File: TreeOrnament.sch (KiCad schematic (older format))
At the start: 29 parts, among them J1 USB_B_Micro

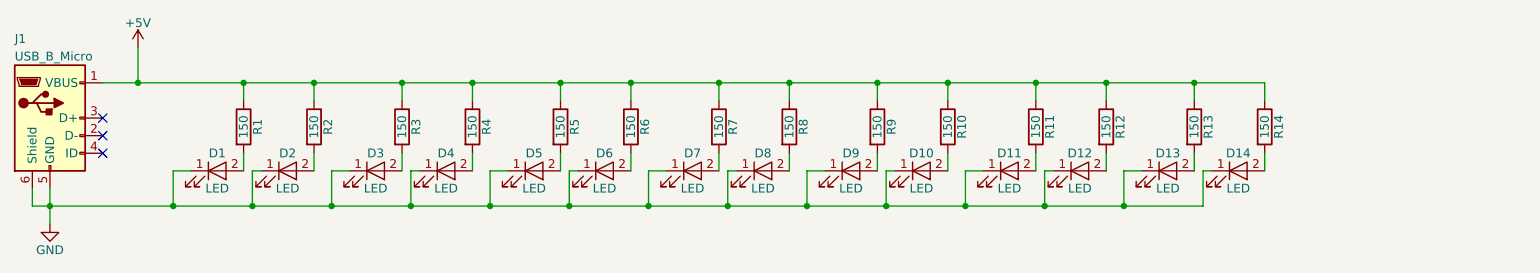
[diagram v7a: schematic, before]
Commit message: Add some optional SMT decoupling caps.
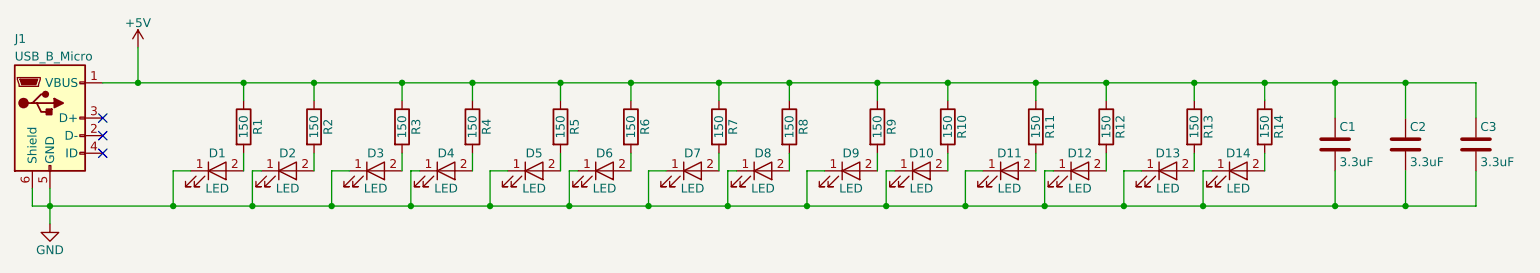
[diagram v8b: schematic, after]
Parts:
- added C1, C2, C3: 3.3uF, Capacitors_SMD:C_0805_HandSoldering, symbol C
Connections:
- net +5V: now also C1.1, C2.1, C3.1
- net GND: now also C1.2, C2.2, C3.2
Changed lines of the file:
@@
 encoding utf-8
 Sheet 1 1
-Title ""
-Date ""
-Rev ""
-Comp ""
+Title "Christmas Tree Ornament"
+Date "2017-11-02"
+Rev "1.1"
+Comp "Patrick Pelletier"
 Comment1 ""
 Comment2 ""
@@
 Connection ~ 6700 1900
 Wire Wire Line
-	1400 1900 8050 1900
-Wire Wire Line
-	1800 1200 8400 1200
+	1400 1900 9600 1900
+Wire Wire Line
+	1800 1200 9600 1200
 $Comp
 L R R1
@@
 	8050 1700 8050 1900
 Connection ~ 7600 1900
+$Comp
+L C C1
+U 1 1 59FBC6D7
+P 8800 1550
+F 0 "C1" H 8825 1650 50  0000 L CNN
+F 1 "3.3uF" H 8825 1450 50  0000 L CNN
+F 2 "Capacitors_SMD:C_0805_HandSoldering" H 8838 1400 50  0001 C CNN
+F 3 "" H 8800 1550 50  0001 C CNN
+	1    8800 1550
+	1    0    0    -1
+$EndComp
+$Comp
+L C C2
+U 1 1 59FBC804
+P 9200 1550
+F 0 "C2" H 9225 1650 50  0000 L CNN
+F 1 "3.3uF" H 9225 1450 50  0000 L CNN
+F 2 "Capacitors_SMD:C_0805_HandSoldering" H 9238 1400 50  0001 C CNN
+F 3 "" H 9200 1550 50  0001 C CNN
+	1    9200 1550
+	1    0    0    -1
+$EndComp
+$Comp
+L C C3
+U 1 1 59FBC875
+P 9600 1550
+F 0 "C3" H 9625 1650 50  0000 L CNN
+F 1 "3.3uF" H 9625 1450 50  0000 L CNN
+F 2 "Capacitors_SMD:C_0805_HandSoldering" H 9638 1400 50  0001 C CNN
+F 3 "" H 9600 1550 50  0001 C CNN
+	1    9600 1550
+	1    0    0    -1
+$EndComp
+Wire Wire Line
+	8800 1200 8800 1400
+Connection ~ 8400 1200
+Wire Wire Line
+	9200 1200 9200 1400
+Connection ~ 8800 1200
+Wire Wire Line
+	9600 1200 9600 1400
+Connection ~ 9200 1200
+Wire Wire Line
+	9600 1900 9600 1700
+Connection ~ 8050 1900
+Wire Wire Line
+	8800 1700 8800 1900
+Connection ~ 8800 1900
+Wire Wire Line
+	9200 1700 9200 1900
+Connection ~ 9200 1900
 $EndSCHEMATC
